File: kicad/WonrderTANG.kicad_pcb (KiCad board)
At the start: 2 copper layers, 101.6 x 90.2 mm, 31 parts, among them CON1 MSX-CONNECTOR, J1 Conn_02x01, J2 AudioJack3, J3 Conn_02x01, Q1 2N3904, U1 SN74LVC245AN, U2 SN74LVC245AN, U3 SN74LVC245AN, U4 SN74LVC245AN, U5 Tang_Nano_20k, U6 SN74LVC245AN

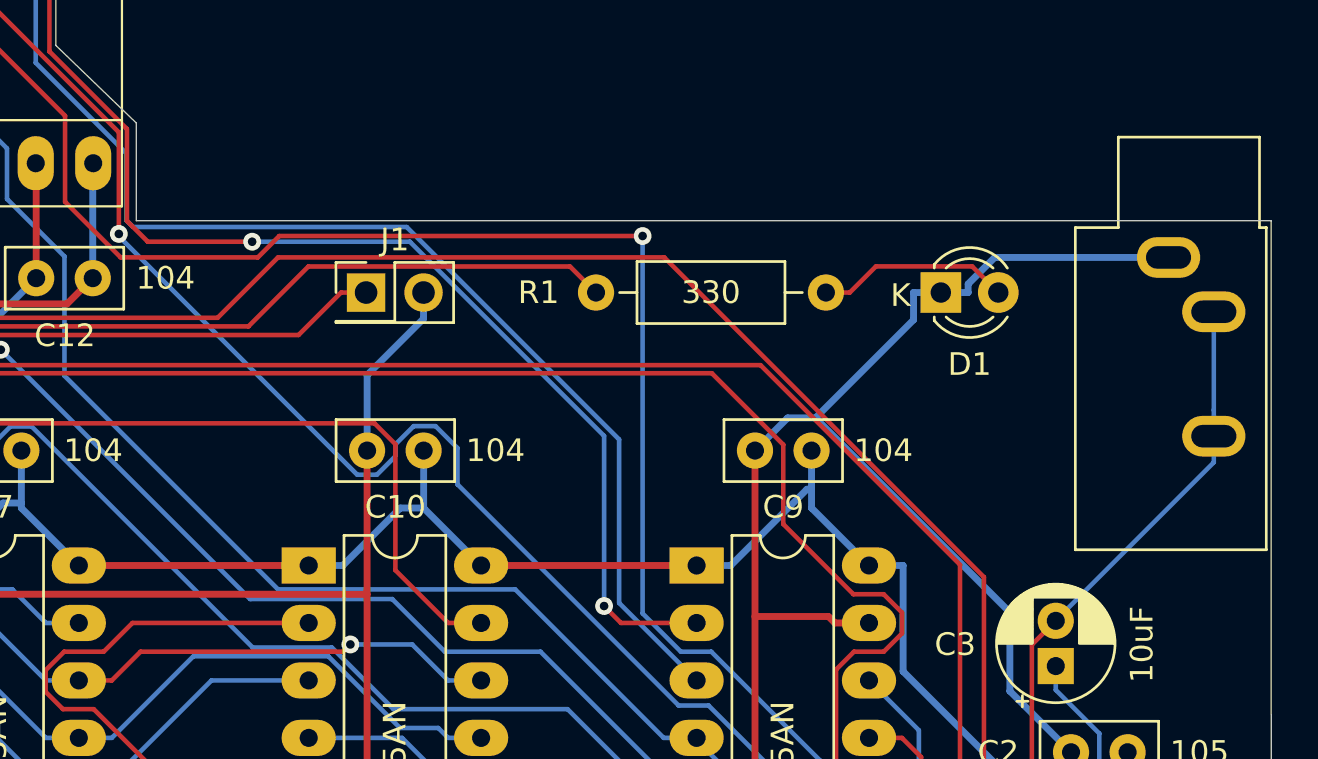
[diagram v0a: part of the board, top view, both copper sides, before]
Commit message: [kicad] Use alternate audio connector SJ1-3525N
Exchange the SJ1-3533NG mono audio connector with the more common
(at least in Europe and some large asian shops) SJ1-3525N stereo
connector, keeping the same orientation.
To fit the new connector the board led is slightly moved too.

Signed-off-by: Albert Herranz <albert_herranz@yahoo.es>
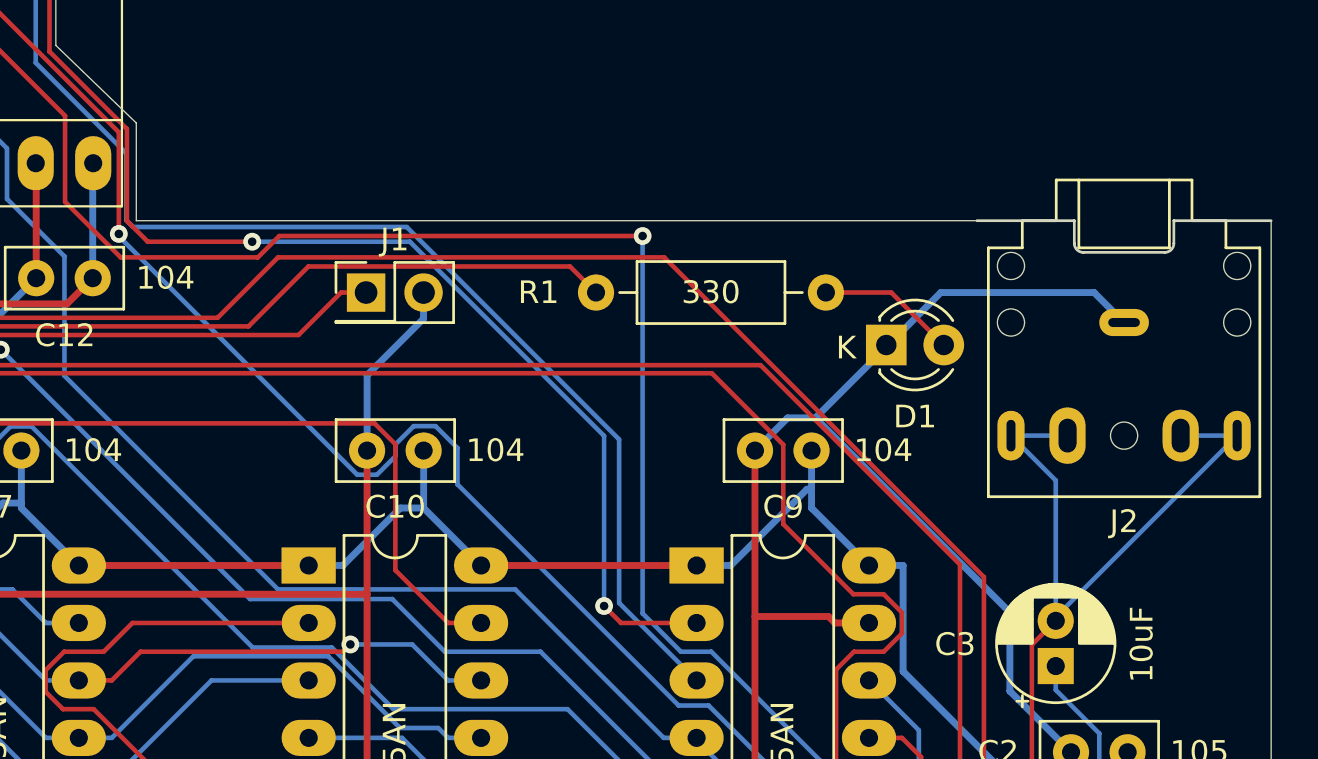
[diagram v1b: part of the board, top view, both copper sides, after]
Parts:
- J2: footprint Connector_Audio:Jack_3.5mm_CUI_SJ1-3533NG_Horizontal -> Connector_Audio:Jack_3.5mm_CUI_SJ1-3525N_Horizontal
- moved J2 3.48 mm to (151.6, 82.6), turned to 180 degrees
- moved D1 3.35 mm to (141.1, 83.6)
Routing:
- net /AUDIO: track 183.1 -> 192.1 mm
- net GND: track 409.1 -> 406.2 mm
- net Net-(D1-A): track 8.58 -> 6.17 mm
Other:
- outline, holes or cut-outs redrawn

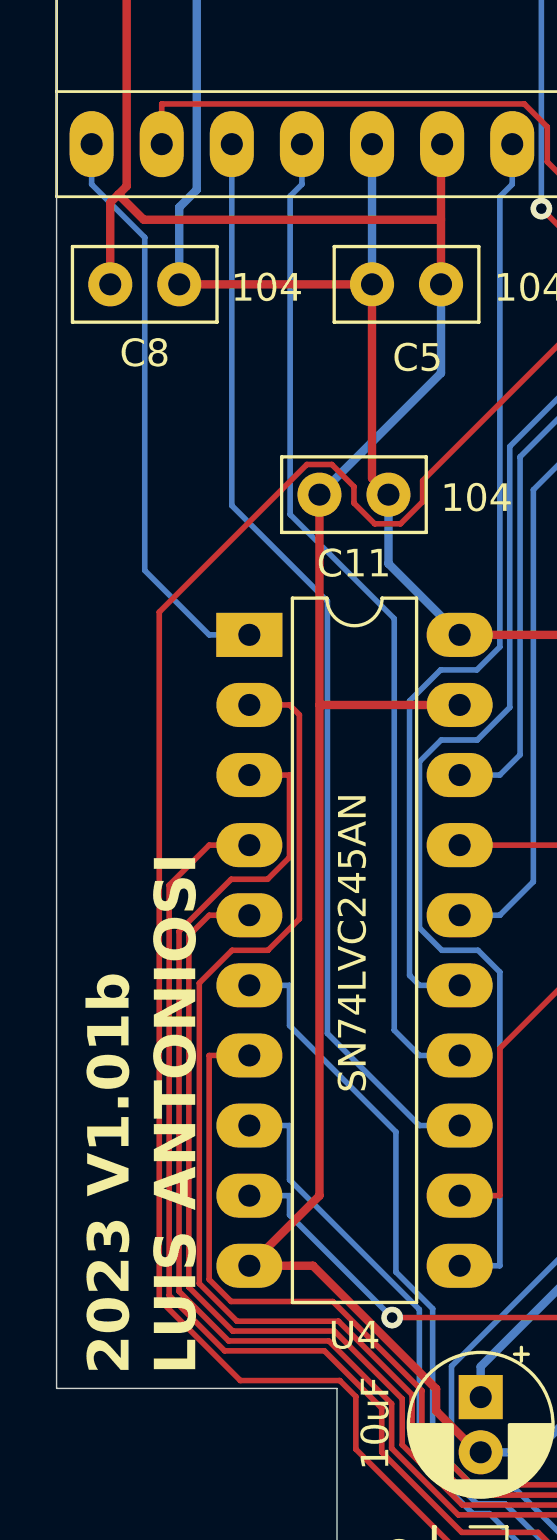
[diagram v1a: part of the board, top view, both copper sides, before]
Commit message: [kicad] Mark board as F1 fork
Identify this board as a new fork to avoid confusion with the stock
board by slightly changing the silkscreen identification.

Signed-off-by: Albert Herranz <albert_herranz@yahoo.es>
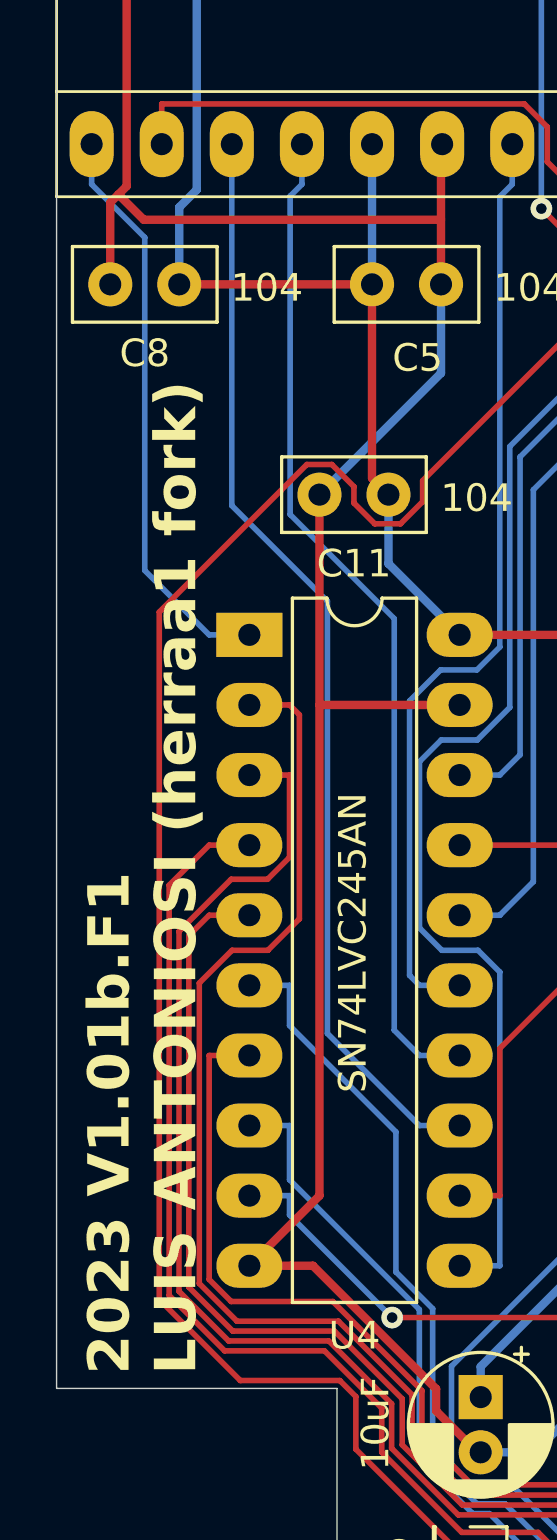
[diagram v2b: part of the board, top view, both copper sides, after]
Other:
- board text added: "2023 V1.01b.F1 LUIS ANTONIOSI (herraa1 fork)"
- board text removed: "2023 V1.01b LUIS ANTONIOSI"
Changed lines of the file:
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@@
     (effects (font (size 1 1) (thickness 0.15)))
   )
-  (gr_text "2023 V1.01b\nLUIS ANTONIOSI" (at 61.722 120.142 90) (layer "F.SilkS")
+  (gr_text "2023 V1.01b.F1\nLUIS ANTONIOSI (herraa1 fork)" (at 61.722 120.142 90) (layer "F.SilkS")
     (effects (font (size 1.5 1.5) (thickness 0.3) bold) (justify left bottom))
   )

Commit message: Release 2023 V1.01b.F1
Add copper planes for final fabrication.

Signed-off-by: Albert Herranz <albert_herranz@yahoo.es>
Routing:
- added copper zone on B.Cu, net GND
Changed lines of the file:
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@@
   )
   (layers
-    (0 "F.Cu" signal "Top")
-    (31 "B.Cu" signal "Bottom")
+    (0 "F.Cu" signal)
+    (31 "B.Cu" signal)
     (32 "B.Adhes" user "B.Adhesive")
     (33 "F.Adhes" user "F.Adhesive")
@@
       (plot_on_all_layers_selection 0x0000000_00000000)
       (disableapertmacros false)
-      (usegerberextensions false)
-      (usegerberattributes true)
-      (usegerberadvancedattributes true)
+      (usegerberextensions true)
+      (usegerberattributes false)
+      (usegerberadvancedattributes false)
       (creategerberjobfile false)
       (dashed_line_dash_ratio 12.000000)
@@
       (net 1 "+3.3V") (pinfunction "3V3") (pintype "bidirectional"))
     (pad "26" thru_hole oval (at 20.32 35.56 270) (size 2.4 1.6) (drill 0.8) (layers "*.Cu" "*.Mask")
-      (net 2 "GND") (pinfunction "GND") (pintype "bidirectional"))
+      (net 2 "GND") (pinfunction "GND") (pintype "bidirectional") (thermal_bridge_angle 45))
     (pad "27" thru_hole oval (at 20.32 33.02 270) (size 2.4 1.6) (drill 0.8) (layers "*.Cu" "*.Mask")
       (net 56 "D3_33") (pinfunction "79_IOT27B") (pintype "bidirectional"))
@@
       )
     )
+  )
+  (zone (net 2) (net_name "GND") (layer "B.Cu") (hatch edge 0.5)
+    (connect_pads (clearance 0.3508))
+    (min_thickness 0.25) (filled_areas_thickness no)
+    (fill yes (thermal_gap 0.5) (thermal_bridge_width 0.5))
+    (polygon
+      (pts
+        (xy 56.6 53.4)
+        (xy 107.9 53.4)
+        (xy 107.9 57.1)
+        (xy 104.3 60.6)
+        (xy 104.3 70.4)
+        (xy 107.9 73.9)
+        (xy 107.9 78.2)
+        (xy 158 78.2)
+        (xy 158 133.3)
+        (xy 78.8 133.3)
+        (xy 66.8 133.2)
+        (xy 66.8 120.6)
+        (xy 56.6 120.6)
+      )
+    )
